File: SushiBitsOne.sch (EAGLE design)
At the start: 57 parts, among them IC1 CH340B, IC2 LM3671-3.3DBV, IC3 TPS562200DBV, J1 ARDUINO_R3, J2 DC-005, Q1 2N7002, Q2 MMBT2222A, U1 STM32F103CBT6-LQFP48, X1 32768Hz, X2 8MHz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

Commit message: Release: M193v3
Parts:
- added L3: (no value), rcl:L-EUL2012C
- X1: device Seeed-OPL-crystal-osctllator:CRYSTAL'9133' -> SparkFun-Clocks:CRYSTALSMD-3.2X1.5
- X2: device Seeed-OPL-crystal-osctllator:CRYSTAL'HC49US' -> SparkFun-Clocks:CRYSTALSMD-5X3.2-4PAD
- X3: device con-molex:87758-1016 -> con-leotronics:1365-10
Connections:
- new net N$20: C8.1, L3.2, U1.VDDA
- net +3V3: now also L3.1; no longer C8.1, U1.VDDA
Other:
- note added: "Copyright (c) 2016-2017 Max Chan Open Source Hardware. Released under 3-caluse BSD license"
- note added: "SushiBits M193v3"
- note removed: "Copyright (c) 2016 Max Chan Open Source Hardware. Released under 3-caluse BSD license"
- note removed: "SushiBits M193v1"
- moved on the sheet: BAT1, C1, C2, C3, C4, C5, C6, C7, C8, JP1, L1, L2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

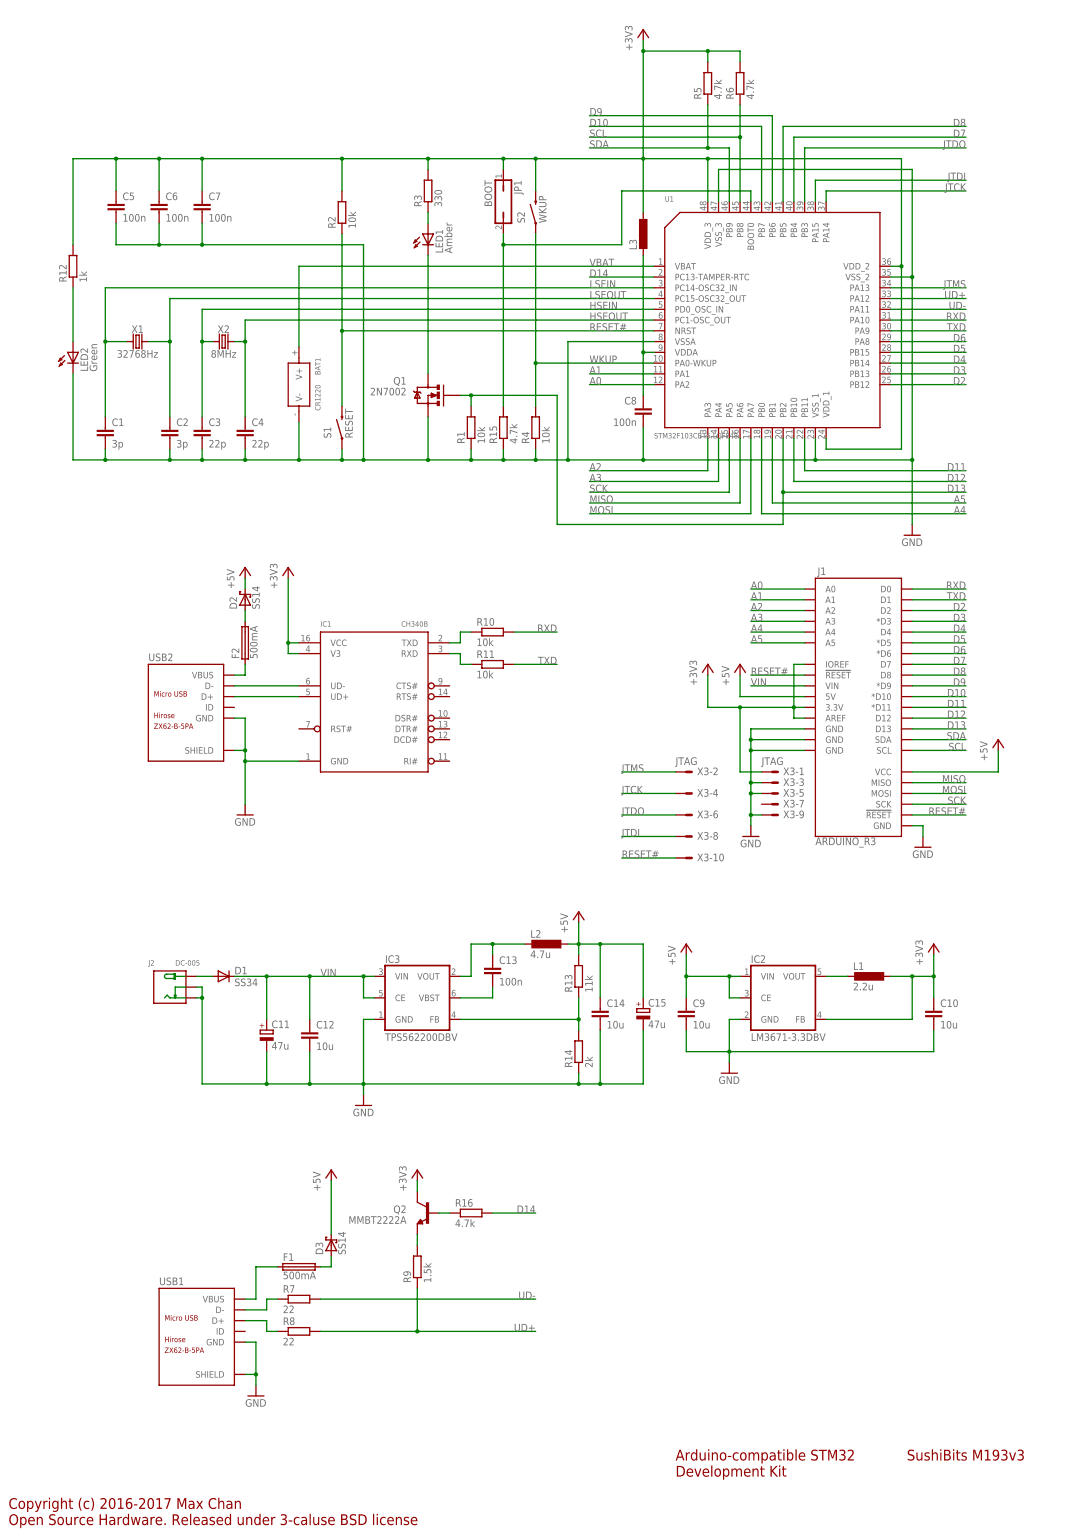
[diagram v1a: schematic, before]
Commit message: Relayout the board to accomodate component changes.
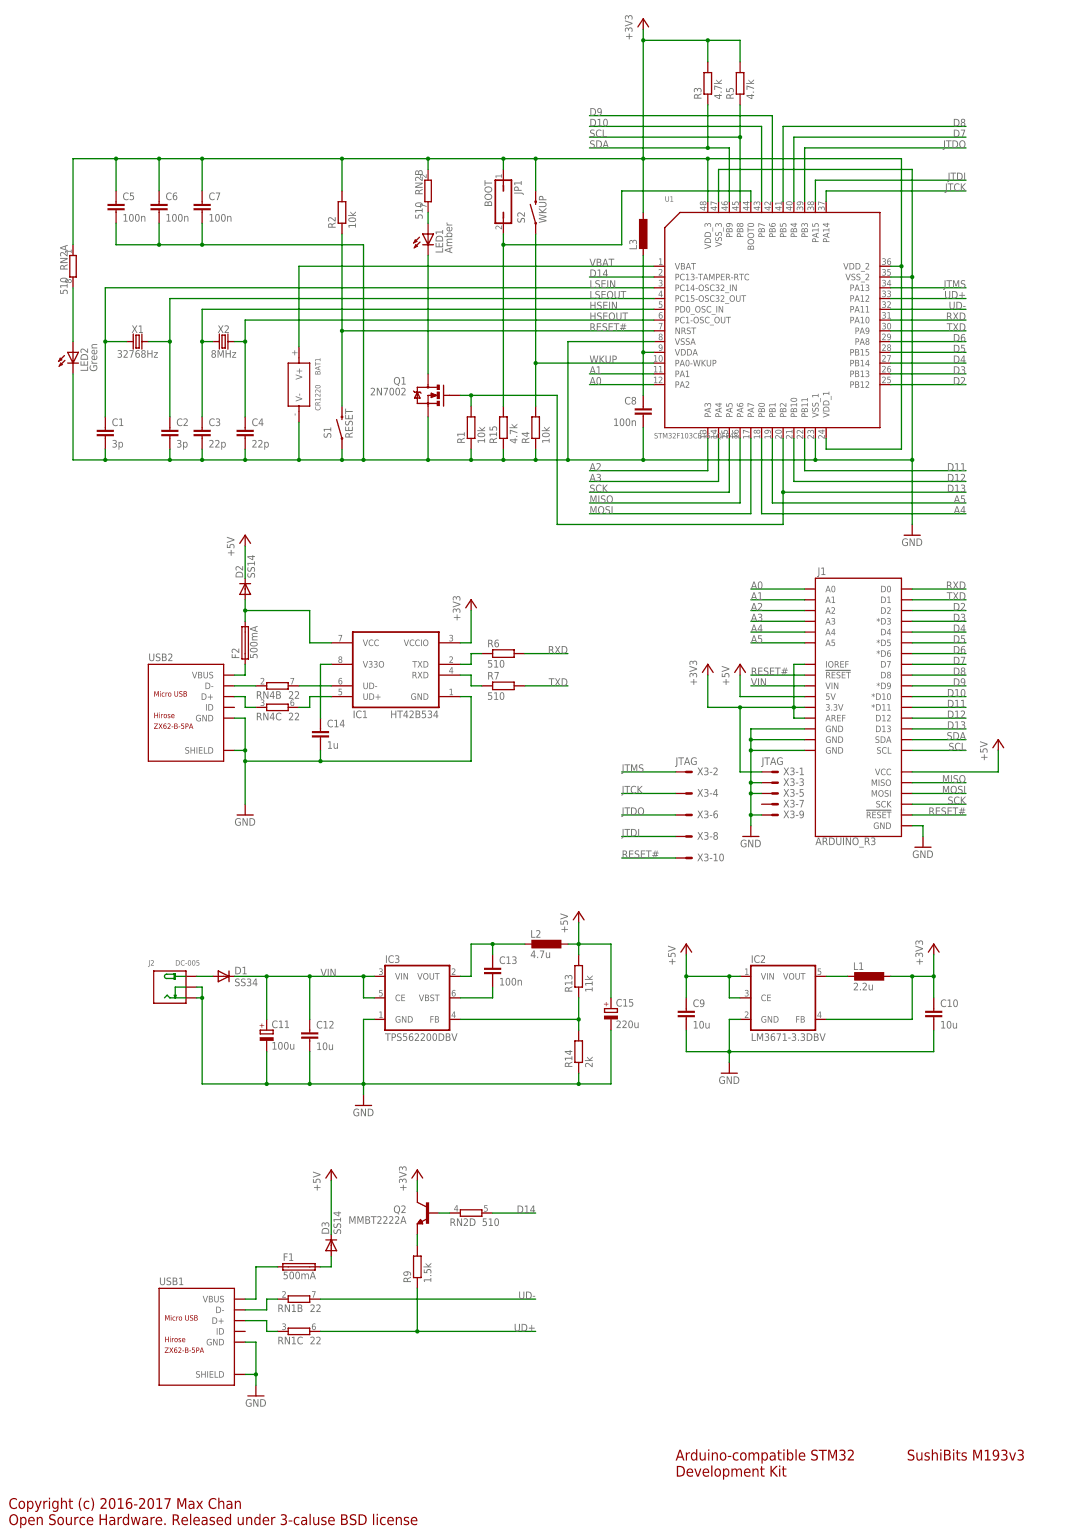
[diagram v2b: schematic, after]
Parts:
- removed R10, R11: 10k, rcl:R-EU_R0603
- removed R12: 1k, rcl:R-EU_R0603
- removed R16: 4.7k, rcl:R-EU_R0603
- removed R8: 22, rcl:R-EU_R0603
- added RN1, RN4: 22, resistor-dil:4R-NEXB38V
- added RN2: 510, resistor-dil:4R-NEXB38V
- C11: value 47u -> 100u; device rcl:CPOL-EUSMCD -> rcl:CPOL-EUUD-6,3X7,7
- C14: value 10u -> 1u; device rcl:C-EUC0805 -> rcl:C-EUC0603
- C15: value 47u -> 220u; device rcl:CPOL-EUSMCB -> rcl:CPOL-EUUD-6,3X8,8
- D2, D3: device diode:SCHOTTKY-DIODEDO214AC -> diode:DIODE-SOD123
- IC1: value CH340B -> HT42B534; device WCH:CH340B -> HT42B534:HT42B534
- R3: value 330 -> 4.7k
- R6: value 4.7k -> 510
- R7: value 22 -> 510
- X2: device SparkFun-Clocks:CRYSTALSMD-5X3.2-4PAD -> SparkFun-Clocks:CRYSTALSMD-5X3.2-2PAD
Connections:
- new net N$21: C14.1, IC1.V33O
- new net N$22: RN4C.1, USB2.D+
- new net N$23: RN4B.1, USB2.D-
- net +3V3: now also IC1.VCCIO, RN2A.1, RN2B.1; no longer IC1.V3, IC1.VCC, R12.2, R6.2
- net +5V: no longer C14.1
- net D14: now also RN2D.2; no longer R16.2
- net N$1: now also RN1B.1; no longer R7.1
- net N$16: now also IC1.VCC
- net N$19: now also RN2D.1; no longer R16.1
- net N$2: now also RN1C.1; no longer R8.1
- net N$3: now also RN4B.2; no longer USB2.D-
- net N$4: now also RN4C.2; no longer USB2.D+
- net N$5: now also R6.1; no longer R10.1
- net N$6: now also R7.1; no longer R11.1
- net N$7: now also RN2A.2; no longer R12.1
- net N$9: now also RN2B.2; no longer R3.1
- net RXD: now also R6.2; no longer R10.2
- net SCL: now also R5.1; no longer R6.1
- net SDA: now also R3.1; no longer R5.1
- net TXD: now also R7.2; no longer R11.2
- net UD+: now also RN1C.2; no longer R8.2
- net UD-: now also RN1B.2; no longer R7.2
- net VBUS: now also F2.1, USB2.VBUS; no longer F1.1, USB1.VBUS
- net VBUS2: now also F1.1, USB1.VBUS; no longer F2.1, USB2.VBUS
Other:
- moved on the sheet: C14, C15, R3, R5, R6, R7

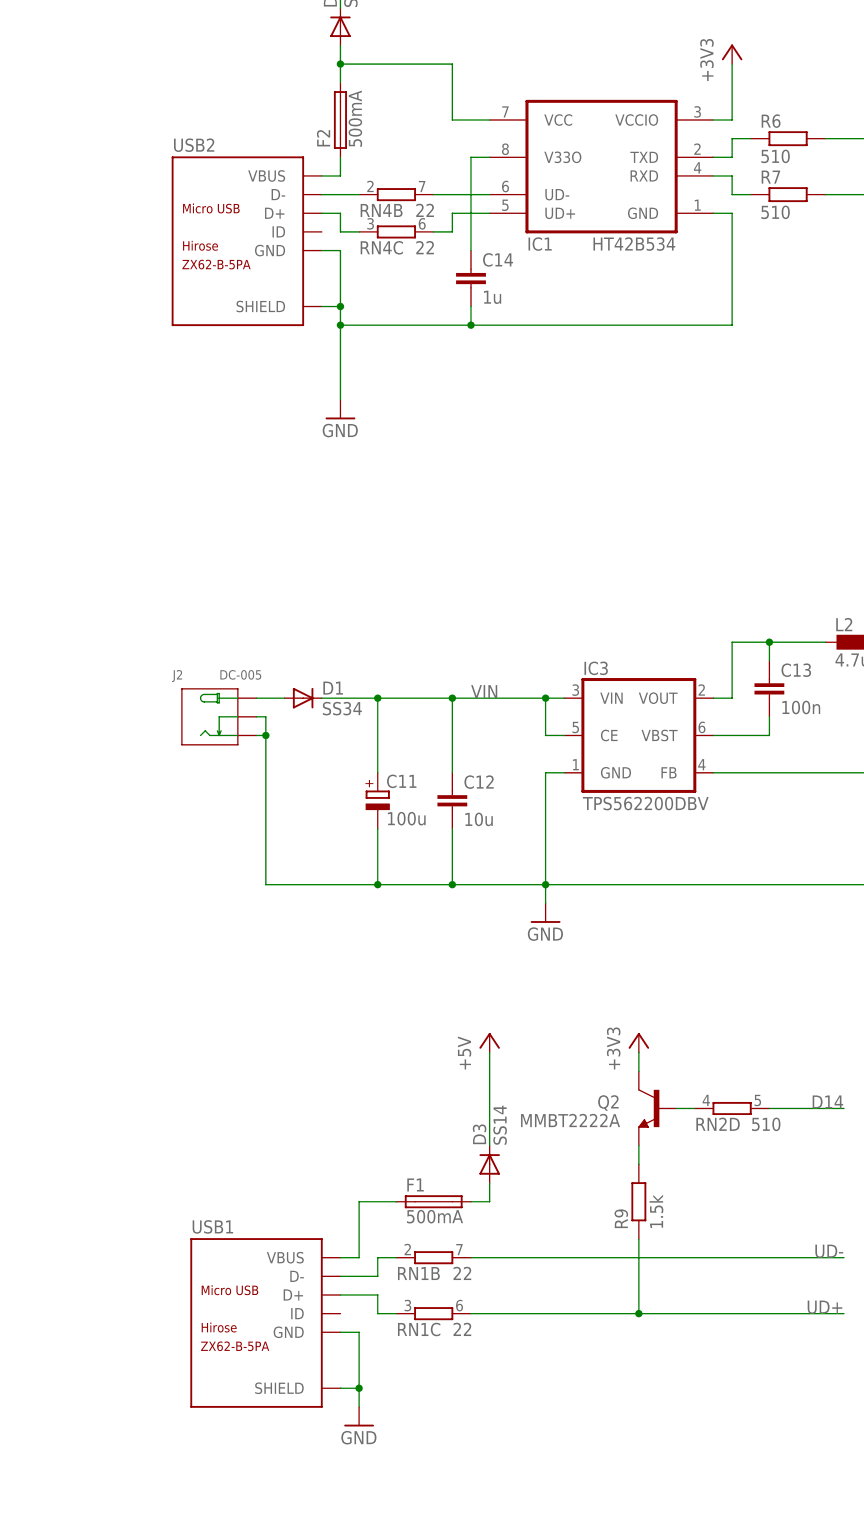
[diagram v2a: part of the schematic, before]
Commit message: Change up some footprints.
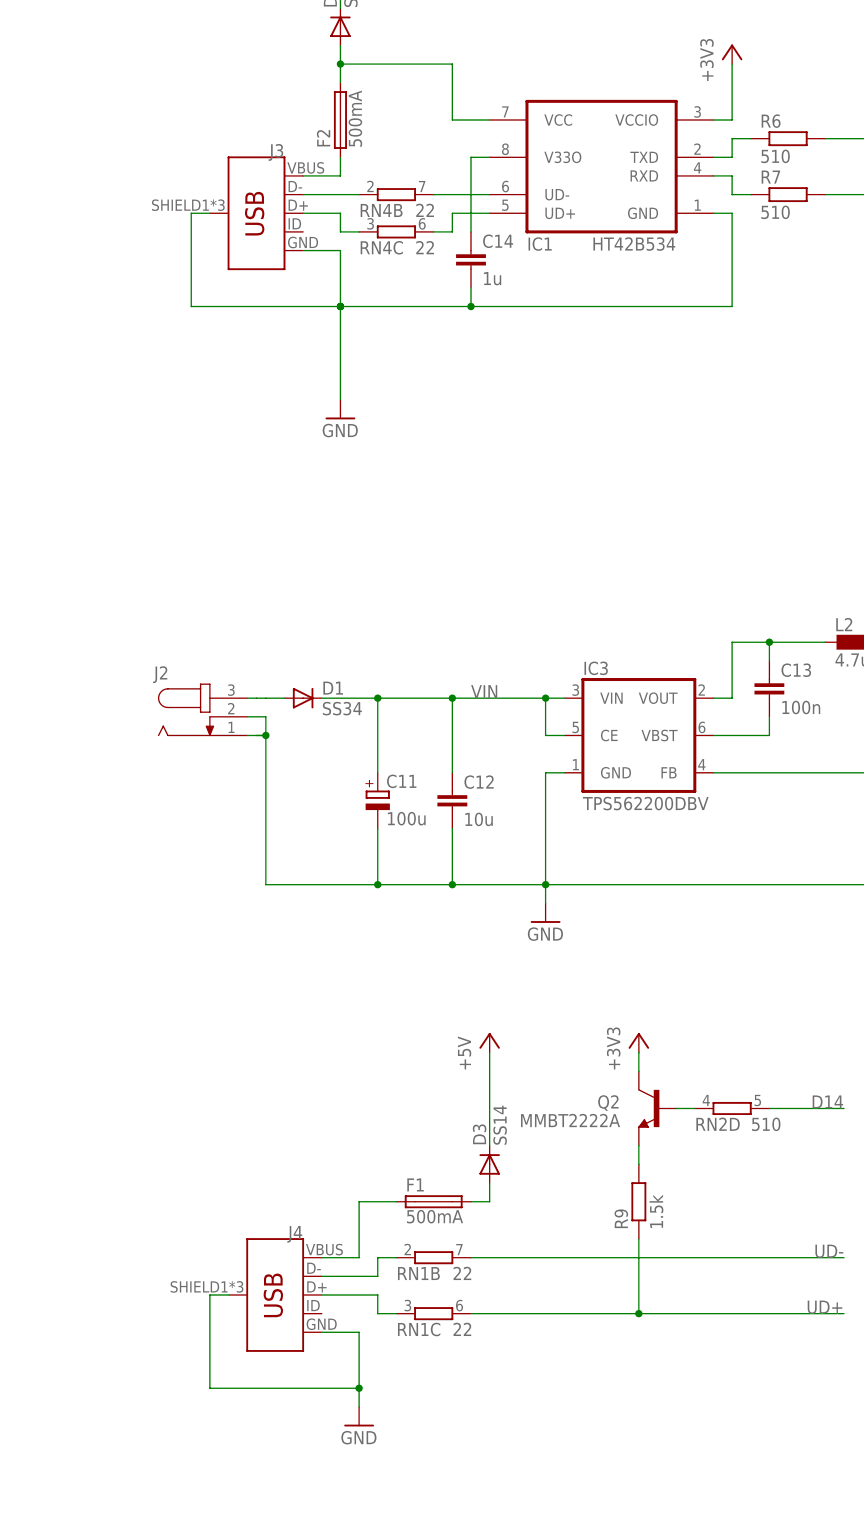
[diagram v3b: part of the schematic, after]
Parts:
- removed USB1, USB2: ZX62-B-5PA, Seeed-OPL-Connector:MICRO-USB-SMD(ZX62-B-5PA)
- added J3, J4: (no value), SparkFun-Connectors:USB_MICRO-B_FEMALE-SMT
- J2: value DC-005 -> (none); device Seeed-OPL-Connector:CONN-POWER-JACK-2.1MM(DC-005) -> con-jack:JACK-PLUG0
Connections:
- removed net VBUS: F2.1, USB2.VBUS
- new net N$24: F2.1, J3.VBUS
- net GND: now also J2.1, J2.2, J3.GND, J3.SHIELD, J4.GND, J4.SHIELD; no longer J2.-, J2.CDN, USB1.GND, USB1.SHIELD, USB2.GND, USB2.SHIELD
- net N$1: now also J4.D-; no longer USB1.D-
- net N$11: now also J2.3; no longer J2.+
- net N$2: now also J4.D+; no longer USB1.D+
- net N$22: now also J3.D+; no longer USB2.D+
- net N$23: now also J3.D-; no longer USB2.D-
- net VBUS2: now also J4.VBUS; no longer USB1.VBUS
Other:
- moved on the sheet: C14

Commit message: Some manufacturability and cleanup work
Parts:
- C11: device rcl:CPOL-EUUD-6,3X7,7 -> rcl:CPOL-EUUD-8X10
- C15: device rcl:CPOL-EUUD-6,3X8,8 -> rcl:CPOL-EUSMCB
- D1: device diode:DIODE-DO-214AC -> diode:DIODE-DO214AC
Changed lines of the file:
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@@
 <part name="+3V5" library="supply1" deviceset="+3V3" device=""/>
 <part name="P+5" library="supply1" deviceset="+5V" device=""/>
-<part name="D1" library="diode" deviceset="DIODE-" device="DO-214AC" value="SS34"/>
+<part name="D1" library="diode" deviceset="DIODE-" device="DO214AC" value="SS34"/>
 <part name="IC3" library="stm32f103c-dvk2" deviceset="TPS56*200" device="DBV" technology="2"/>
-<part name="C11" library="rcl" deviceset="CPOL-EU" device="UD-6,3X7,7" value="100u"/>
+<part name="C11" library="rcl" deviceset="CPOL-EU" device="UD-8X10" value="100u"/>
 <part name="C12" library="rcl" deviceset="C-EU" device="C0805" value="10u"/>
 <part name="GND7" library="supply1" deviceset="GND" device=""/>
@@
 <part name="R14" library="rcl" deviceset="R-EU_" device="R0603" value="2k"/>
 <part name="P+6" library="supply1" deviceset="+5V" device=""/>
-<part name="C15" library="rcl" deviceset="CPOL-EU" device="UD-6,3X8,8" value="220u"/>
+<part name="C15" library="rcl" deviceset="CPOL-EU" device="SMCB" value="220u"/>
 <part name="R15" library="rcl" deviceset="R-EU_" device="R0603" value="4.7k"/>
 <part name="JP1" library="jumper" deviceset="JP1Q" device="" value="BOOT"/>
